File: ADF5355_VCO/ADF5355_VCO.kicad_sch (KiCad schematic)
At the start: 0 parts

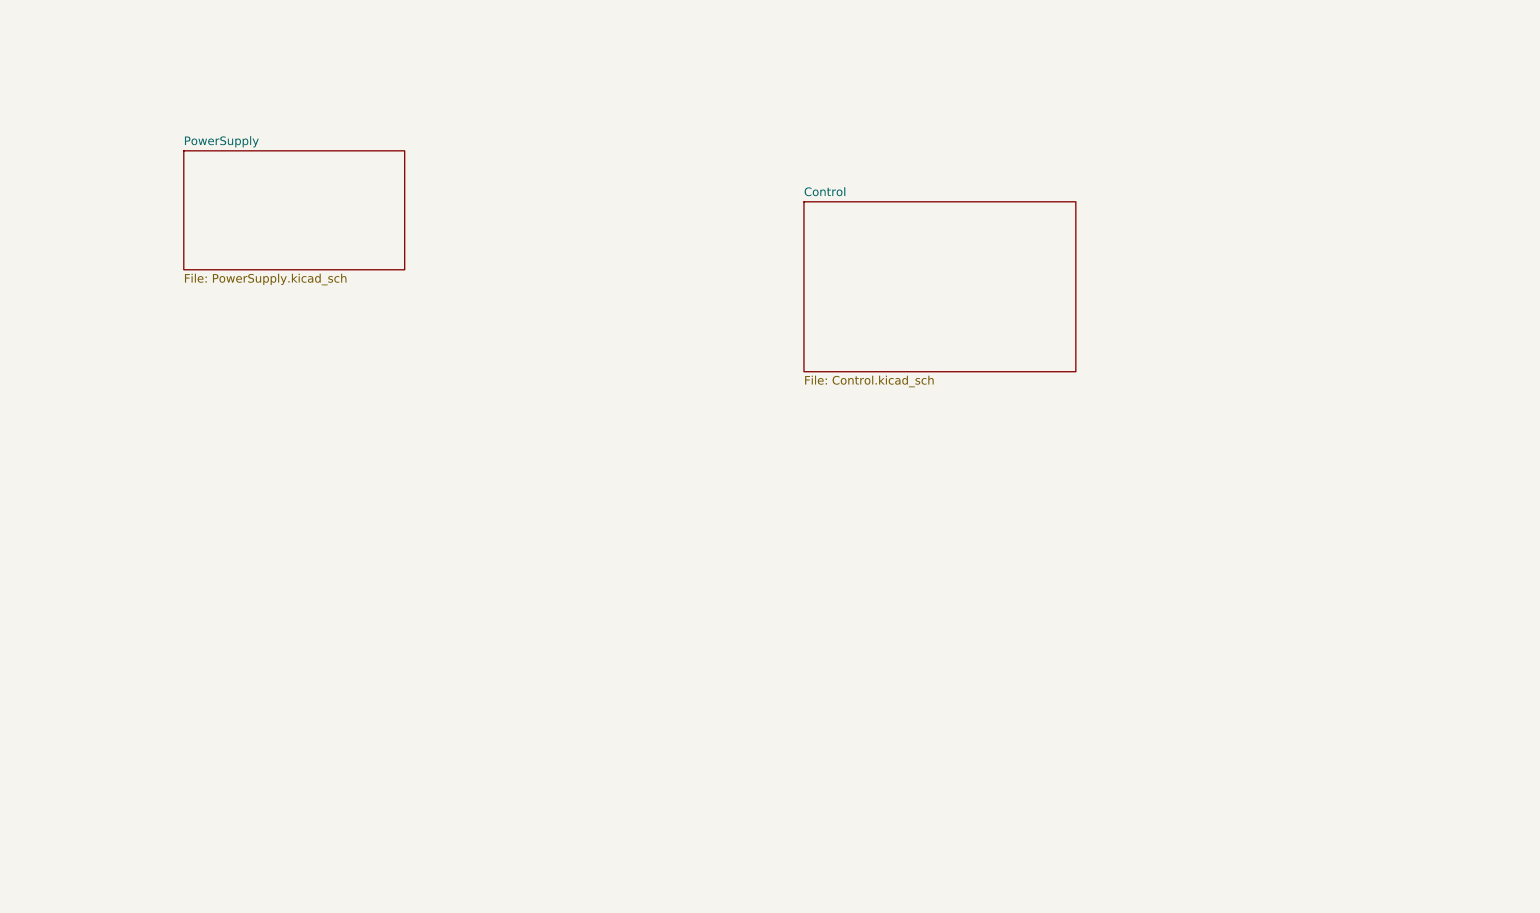
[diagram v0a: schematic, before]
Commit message: ¸Added USB connector and changed connections
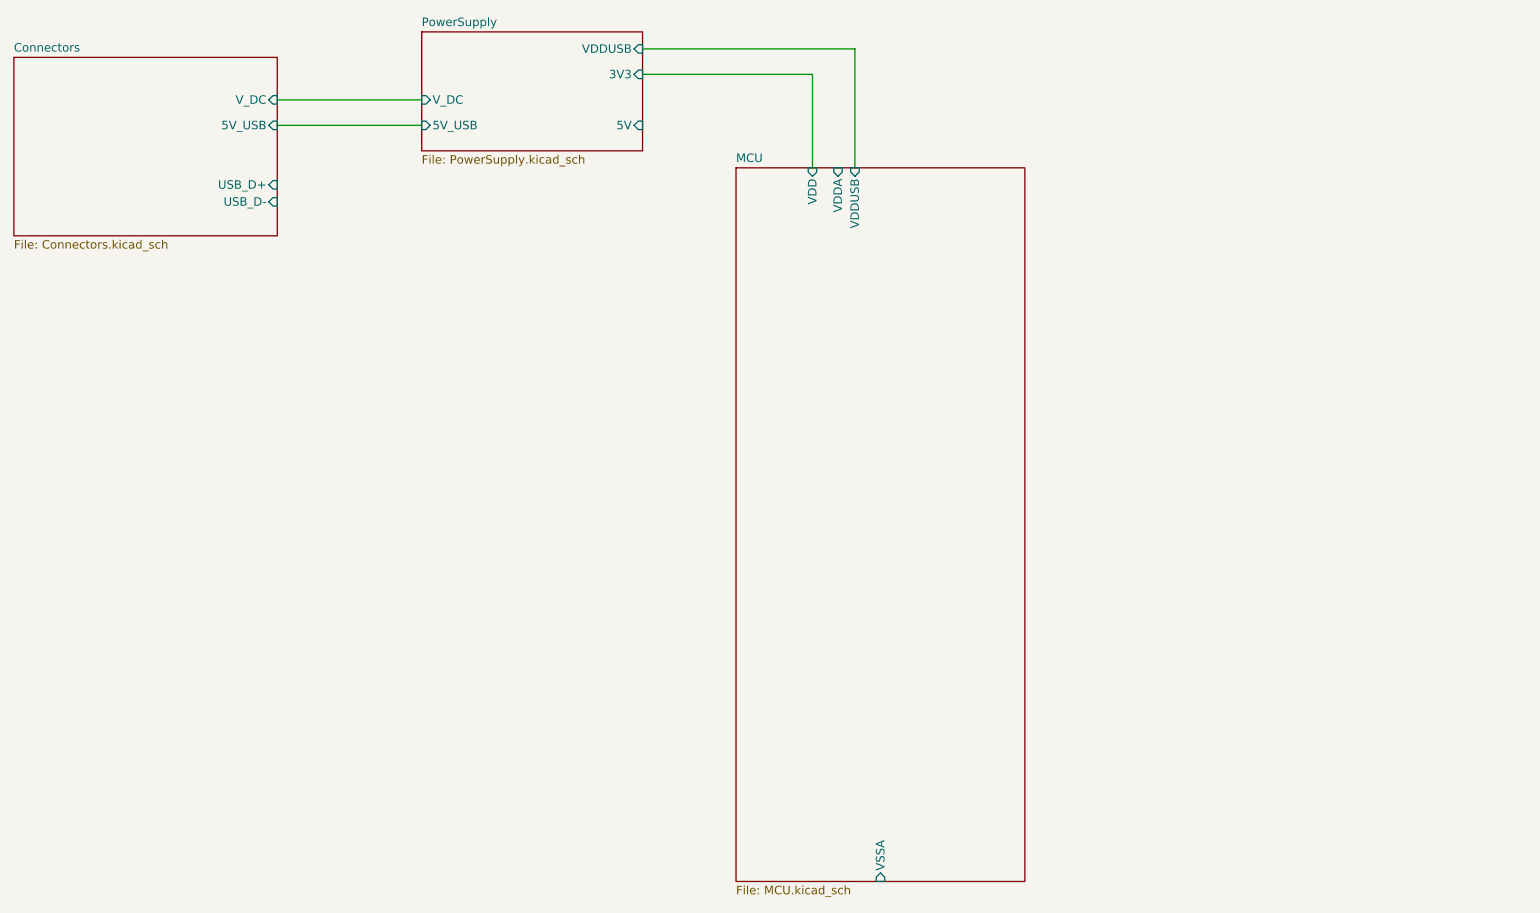
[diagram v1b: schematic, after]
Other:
- sheet Control renamed MCU
- added sheet Connectors (Connectors.kicad_sch)
- sheet MCU: file Control.kicad_sch -> MCU.kicad_sch
- sheet MCU ports: added VDD, VDDA, VDDUSB, VSSA; removed none
- sheet PowerSupply ports: added 3V3, 5V, 5V_USB, VDDUSB, V_DC; removed none
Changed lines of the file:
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@@
 (kicad_sch (version 20230121) (generator eeschema)
   (paper "A4")
-  (sheet (at 45.72 41.91) (size 33.02 17.78) (fields_autoplaced)
+  (wire (pts (xy 114.3 26.67) (xy 146.05 26.67))
+    (stroke (width 0) (type default))
+  )
+  (wire (pts (xy 59.69 34.29) (xy 81.28 34.29))
+    (stroke (width 0) (type default))
+  )
+  (wire (pts (xy 59.69 38.1) (xy 81.28 38.1))
+    (stroke (width 0) (type default))
+  )
+  (wire (pts (xy 139.7 30.48) (xy 139.7 44.45))
+    (stroke (width 0) (type default))
+  )
+  (wire (pts (xy 114.3 30.48) (xy 139.7 30.48))
+    (stroke (width 0) (type default))
+  )
+  (wire (pts (xy 146.05 26.67) (xy 146.05 44.45))
+    (stroke (width 0) (type default))
+  )
+  (sheet (at 81.28 24.13) (size 33.02 17.78) (fields_autoplaced)
     (stroke (width 0) (type solid))
-    (fill (color 0 0 0 0.0000))
-    (property "Sheetname" "PowerSupply" (at 45.72 41.1984 0)
+    (fill (color 255 240 101 1.0000))
+    (property "Sheetname" "PowerSupply" (at 81.28 23.4184 0)
       (effects (font (size 1.27 1.27)) (justify left bottom))
     )
-    (property "Sheetfile" "PowerSupply.kicad_sch" (at 45.72 60.2746 0)
+    (property "Sheetfile" "PowerSupply.kicad_sch" (at 81.28 42.4946 0)
       (effects (font (size 1.27 1.27)) (justify left top))
+    )
+    (pin "3V3" input (at 114.3 30.48 0)
+      (effects (font (size 1.27 1.27)) (justify right))
+    )
+    (pin "5V" input (at 114.3 38.1 0)
+      (effects (font (size 1.27 1.27)) (justify right))
+    )
+    (pin "V_DC" input (at 81.28 34.29 180)
+      (effects (font (size 1.27 1.27)) (justify left))
+    )
+    (pin "5V_USB" input (at 81.28 38.1 180)
+      (effects (font (size 1.27 1.27)) (justify left))
+    )
+    (pin "VDDUSB" input (at 114.3 26.67 0)
+      (effects (font (size 1.27 1.27)) (justify right))
     )
     (instances
@@
     )
   )
-  (sheet (at 138.43 49.53) (size 40.64 25.4) (fields_autoplaced)
+  (sheet (at 128.27 44.45) (size 43.18 106.68) (fields_autoplaced)
     (stroke (width 0.1524) (type solid))
-    (fill (color 0 0 0 0.0000))
-    (property "Sheetname" "Control" (at 138.43 48.8184 0)
+    (fill (color 255 240 101 1.0000))
+    (property "Sheetname" "MCU" (at 128.27 43.7384 0)
       (effects (font (size 1.27 1.27)) (justify left bottom))
     )
-    (property "Sheetfile" "Control.kicad_sch" (at 138.43 75.5146 0)
+    (property "Sheetfile" "MCU.kicad_sch" (at 128.27 151.7146 0)
       (effects (font (size 1.27 1.27)) (justify left top))
+    )
+    (pin "VDD" input (at 139.7 44.45 90)
+      (effects (font (size 1.27 1.27)) (justify right))
+    )
+    (pin "VDDUSB" input (at 146.05 44.45 90)
+      (effects (font (size 1.27 1.27)) (justify right))
+    )
+    (pin "VDDA" input (at 143.51 44.45 90)
+      (effects (font (size 1.27 1.27)) (justify right))
+    )
+    (pin "VSSA" input (at 149.86 151.13 270)
+      (effects (font (size 1.27 1.27)) (justify left))
     )
     (instances
@@
       )
     )
+  )
+  (sheet (at 20.32 27.94) (size 39.37 26.67) (fields_autoplaced)
+    (stroke (width 0.1524) (type solid))
+    (fill (color 255 241 101 1.0000))
+    (property "Sheetname" "Connectors" (at 20.32 27.2284 0)
+      (effects (font (size 1.27 1.27)) (justify left bottom))
+    )
+    (property "Sheetfile" "Connectors.kicad_sch" (at 20.32 55.1946 0)
+      (effects (font (size 1.27 1.27)) (justify left top))
+    )
+    (pin "V_DC" input (at 59.69 34.29 0)
+      (effects (font (size 1.27 1.27)) (justify right))
+    )
+    (pin "USB_D-" input (at 59.69 49.53 0)
+      (effects (font (size 1.27 1.27)) (justify right))
+    )
+    (pin "USB_D+" input (at 59.69 46.99 0)
+      (effects (font (size 1.27 1.27)) (justify right))
+    )
+    (pin "5V_USB" input (at 59.69 38.1 0)
+      (effects (font (size 1.27 1.27)) (justify right))
+    )
+    (instances
+      (project "ADF5355_VCO"
+        (path "/29349b68-071c-451b-9b1e-10b5ef7e12a6" (page "4"))
+      )
+    )

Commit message: Finished MCU sheet
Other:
- sheet MCU ports: added LCD_D0...7, SPI_MISO, SPI_MOSI, SPI_NSS, SPI_SCK, USB_DM, USB_DP; removed VSSA
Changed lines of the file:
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@@
 (kicad_sch (version 20230121) (generator eeschema)
   (paper "A4")
+  (wire (pts (xy 116.84 58.42) (xy 128.27 58.42))
+    (stroke (width 0) (type default))
+  )
   (wire (pts (xy 114.3 26.67) (xy 146.05 26.67))
+    (stroke (width 0) (type default))
+  )
+  (wire (pts (xy 119.38 55.88) (xy 128.27 55.88))
+    (stroke (width 0) (type default))
+  )
+  (wire (pts (xy 59.69 46.99) (xy 119.38 46.99))
+    (stroke (width 0) (type default))
+  )
+  (wire (pts (xy 59.69 49.53) (xy 116.84 49.53))
     (stroke (width 0) (type default))
   )
@@
     (stroke (width 0) (type default))
   )
-  (wire (pts (xy 139.7 30.48) (xy 139.7 44.45))
+  (wire (pts (xy 139.7 35.56) (xy 139.7 44.45))
     (stroke (width 0) (type default))
   )
-  (wire (pts (xy 114.3 30.48) (xy 139.7 30.48))
+  (wire (pts (xy 114.3 35.56) (xy 139.7 35.56))
+    (stroke (width 0) (type default))
+  )
+  (wire (pts (xy 116.84 49.53) (xy 116.84 58.42))
     (stroke (width 0) (type default))
   )
   (wire (pts (xy 146.05 26.67) (xy 146.05 44.45))
+    (stroke (width 0) (type default))
+  )
+  (wire (pts (xy 119.38 46.99) (xy 119.38 55.88))
     (stroke (width 0) (type default))
   )
@@
       (effects (font (size 1.27 1.27)) (justify left top))
     )
-    (pin "3V3" input (at 114.3 30.48 0)
+    (pin "3V3" input (at 114.3 35.56 0)
       (effects (font (size 1.27 1.27)) (justify right))
     )
@@
     )
   )
-  (sheet (at 128.27 44.45) (size 43.18 106.68) (fields_autoplaced)
+  (sheet (at 128.27 44.45) (size 43.18 49.53) (fields_autoplaced)
     (stroke (width 0.1524) (type solid))
     (fill (color 255 240 101 1.0000))
-    (property "Sheetname" "MCU" (at 128.27 43.7384 0)
+    (property "Sheetname" "MCU" (at 127.5584 93.98 90)
       (effects (font (size 1.27 1.27)) (justify left bottom))
     )
-    (property "Sheetfile" "MCU.kicad_sch" (at 128.27 151.7146 0)
+    (property "Sheetfile" "MCU.kicad_sch" (at 172.0346 93.98 90)
       (effects (font (size 1.27 1.27)) (justify left top))
     )
@@
       (effects (font (size 1.27 1.27)) (justify right))
     )
-    (pin "VSSA" input (at 149.86 151.13 270)
+    (pin "LCD_D0...7" input (at 128.27 69.85 180)
       (effects (font (size 1.27 1.27)) (justify left))
     )
+    (pin "SPI_MISO" input (at 171.45 63.5 0)
+      (effects (font (size 1.27 1.27)) (justify right))
+    )
+    (pin "SPI_NSS" input (at 171.45 58.42 0)
+      (effects (font (size 1.27 1.27)) (justify right))
+    )
+    (pin "SPI_SCK" input (at 171.45 60.96 0)
+      (effects (font (size 1.27 1.27)) (justify right))
+    )
+    (pin "SPI_MOSI" input (at 171.45 66.04 0)
+      (effects (font (size 1.27 1.27)) (justify right))
+    )
+    (pin "USB_DM" input (at 128.27 58.42 180)
+      (effects (font (size 1.27 1.27)) (justify left))
+    )
+    (pin "USB_DP" input (at 128.27 55.88 180)
+      (effects (font (size 1.27 1.27)) (justify left))
+    )

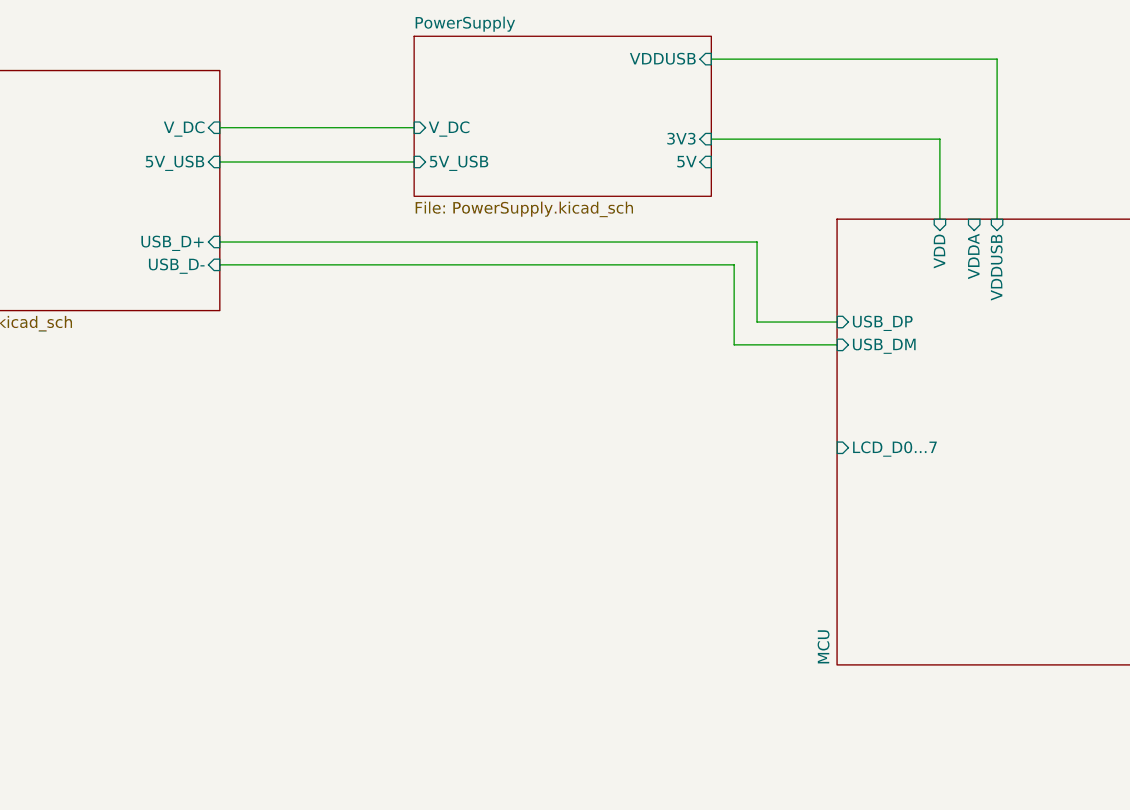
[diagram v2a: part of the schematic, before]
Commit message: Added LCD screen
Added LCD 16x2 screen to the project and modified MCU sheet for using aditional GPIO pins for enable and reset pin.
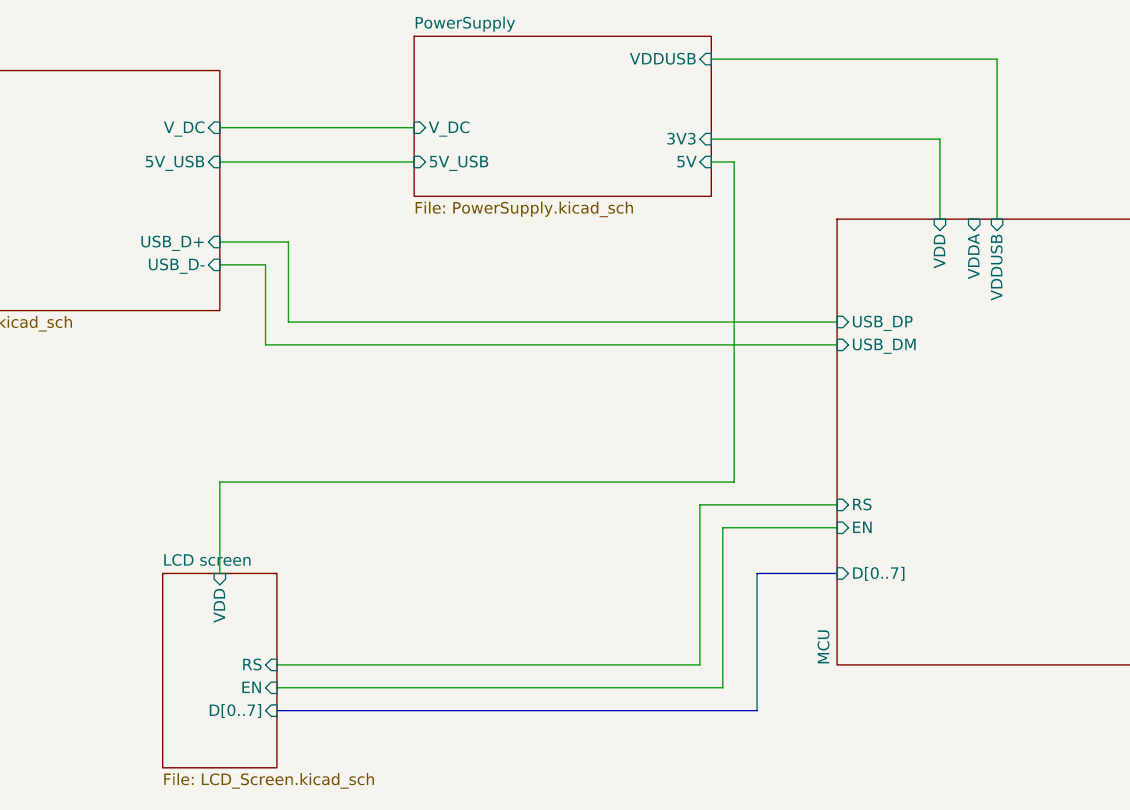
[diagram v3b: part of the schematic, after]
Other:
- added sheet LCD screen (LCD_Screen.kicad_sch)
- sheet MCU ports: added D[0..7], EN, RS; removed LCD_D0...7
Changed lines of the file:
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@@
 (kicad_sch (version 20230121) (generator eeschema)
   (paper "A4")
-  (wire (pts (xy 116.84 58.42) (xy 128.27 58.42))
+  (wire (pts (xy 66.04 96.52) (xy 115.57 96.52))
+    (stroke (width 0) (type default))
+  )
+  (wire (pts (xy 59.69 49.53) (xy 64.77 49.53))
+    (stroke (width 0) (type default))
+  )
+  (wire (pts (xy 115.57 78.74) (xy 115.57 96.52))
+    (stroke (width 0) (type default))
+  )
+  (wire (pts (xy 64.77 49.53) (xy 64.77 58.42))
+    (stroke (width 0) (type default))
+  )
+  (wire (pts (xy 59.69 73.66) (xy 116.84 73.66))
+    (stroke (width 0) (type default))
+  )
+  (wire (pts (xy 66.04 93.98) (xy 113.03 93.98))
+    (stroke (width 0) (type default))
+  )
+  (wire (pts (xy 114.3 38.1) (xy 116.84 38.1))
+    (stroke (width 0) (type default))
+  )
+  (wire (pts (xy 64.77 58.42) (xy 128.27 58.42))
     (stroke (width 0) (type default))
   )
@@
     (stroke (width 0) (type default))
   )
-  (wire (pts (xy 119.38 55.88) (xy 128.27 55.88))
-    (stroke (width 0) (type default))
-  )
-  (wire (pts (xy 59.69 46.99) (xy 119.38 46.99))
-    (stroke (width 0) (type default))
-  )
-  (wire (pts (xy 59.69 49.53) (xy 116.84 49.53))
+  (wire (pts (xy 67.31 55.88) (xy 128.27 55.88))
+    (stroke (width 0) (type default))
+  )
+  (wire (pts (xy 59.69 46.99) (xy 67.31 46.99))
+    (stroke (width 0) (type default))
+  )
+  (wire (pts (xy 113.03 76.2) (xy 113.03 93.98))
+    (stroke (width 0) (type default))
+  )
+  (wire (pts (xy 116.84 38.1) (xy 116.84 73.66))
+    (stroke (width 0) (type default))
+  )
+  (bus (pts (xy 119.38 83.82) (xy 119.38 99.06))
+    (stroke (width 0) (type default))
+  )
+  (wire (pts (xy 128.27 78.74) (xy 115.57 78.74))
     (stroke (width 0) (type default))
   )
@@
     (stroke (width 0) (type default))
   )
-  (wire (pts (xy 116.84 49.53) (xy 116.84 58.42))
+  (wire (pts (xy 59.69 73.66) (xy 59.69 83.82))
+    (stroke (width 0) (type default))
+  )
+  (wire (pts (xy 128.27 76.2) (xy 113.03 76.2))
+    (stroke (width 0) (type default))
+  )
+  (bus (pts (xy 128.27 83.82) (xy 119.38 83.82))
+    (stroke (width 0) (type default))
+  )
+  (bus (pts (xy 66.04 99.06) (xy 119.38 99.06))
     (stroke (width 0) (type default))
   )
@@
     (stroke (width 0) (type default))
   )
-  (wire (pts (xy 119.38 46.99) (xy 119.38 55.88))
+  (wire (pts (xy 67.31 46.99) (xy 67.31 55.88))
     (stroke (width 0) (type default))
   )
@@
       (effects (font (size 1.27 1.27)) (justify right))
     )
-    (pin "LCD_D0...7" input (at 128.27 69.85 180)
+    (pin "D[0..7]" input (at 128.27 83.82 180)
       (effects (font (size 1.27 1.27)) (justify left))
     )
@@
     )
     (pin "USB_DP" input (at 128.27 55.88 180)
+      (effects (font (size 1.27 1.27)) (justify left))
+    )
+    (pin "RS" input (at 128.27 76.2 180)
+      (effects (font (size 1.27 1.27)) (justify left))
+    )
+    (pin "EN" input (at 128.27 78.74 180)
       (effects (font (size 1.27 1.27)) (justify left))
     )
@@
       )
     )
+  )
+  (sheet (at 53.34 83.82) (size 12.7 21.59) (fields_autoplaced)
+    (stroke (width 0.1524) (type solid))
+    (fill (color 255 240 101 1.0000))
+    (property "Sheetname" "LCD screen" (at 53.34 83.1084 0)
+      (effects (font (size 1.27 1.27)) (justify left bottom))
+    )
+    (property "Sheetfile" "LCD_Screen.kicad_sch" (at 53.34 105.9946 0)
+      (effects (font (size 1.27 1.27)) (justify left top))
+    )
+    (property "Field2" "" (at 53.34 83.82 0)
+      (effects (font (size 1.27 1.27)) hide)
+    )
+    (pin "EN" input (at 66.04 96.52 0)
+      (effects (font (size 1.27 1.27)) (justify right))
+    )
+    (pin "RS" input (at 66.04 93.98 0)
+      (effects (font (size 1.27 1.27)) (justify right))
+    )
+    (pin "D[0..7]" input (at 66.04 99.06 0)
+      (effects (font (size 1.27 1.27)) (justify right))
+    )
+    (pin "VDD" input (at 59.69 83.82 90)
+      (effects (font (size 1.27 1.27)) (justify right))
+    )
+    (instances
+      (project "ADF5355_VCO"
+        (path "/29349b68-071c-451b-9b1e-10b5ef7e12a6" (page "5"))
+      )
+    )
